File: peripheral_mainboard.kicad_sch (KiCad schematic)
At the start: 35 parts, among them J5 AudioJack3, J9 FFC Connector, SW2 SW_SPST, SW3 SW_SPST, SW7 SW_SPST, U5 TLV70033_SOT23-5, U6 PCM5102APW, U7 PAM8908

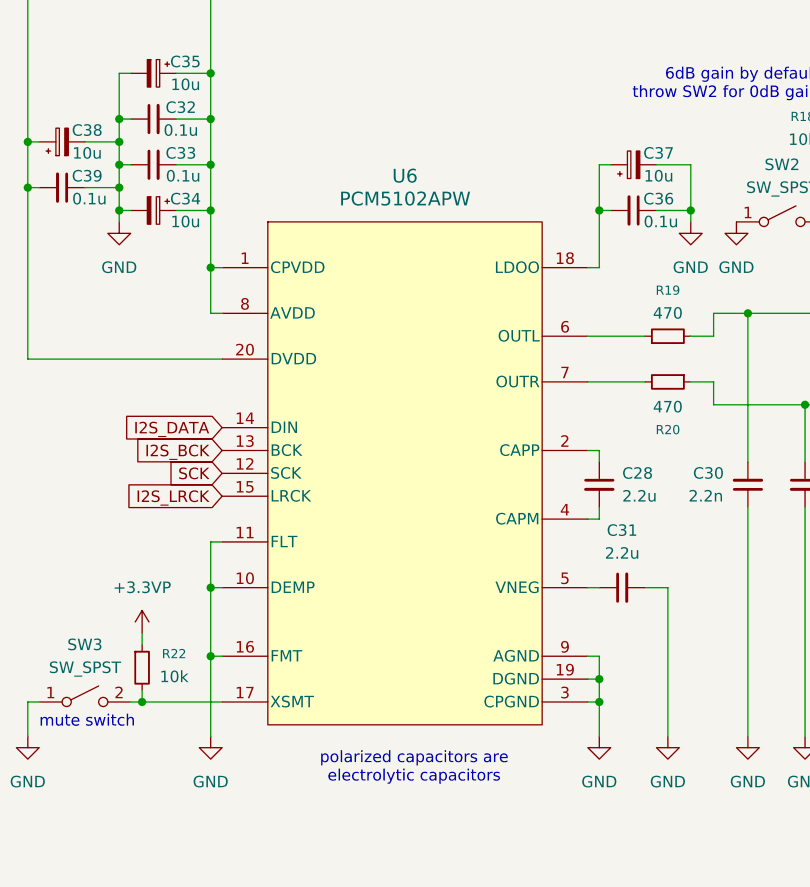
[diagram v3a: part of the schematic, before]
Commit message: removed external footprint/model
these were from ultralibrarian and should never have been included here, my bad
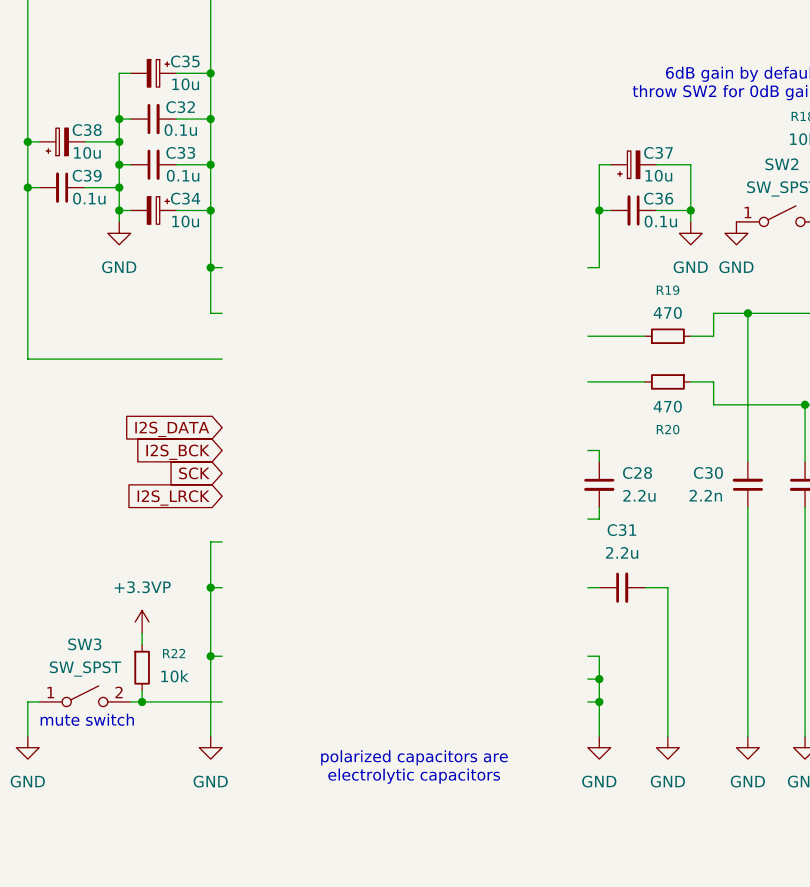
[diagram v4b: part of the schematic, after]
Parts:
- removed U6: PCM5102APW, PCM5102A:PW0020A_L, symbol PCM5102A:PCM5102APW
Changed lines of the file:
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@@
-	)
-	(symbol
-		(lib_id "PCM5102A:PCM5102APW")
-		(at 146.05 100.33 0)
-		(unit 1)
-		(exclude_from_sim no)
-		(in_bom yes)
-		(on_board yes)
-		(dnp no)
-		(fields_autoplaced yes)
-		(property "Reference" "U6"
-			(at 146.05 67.31 0)
-			(effects
-				(font
-					(size 1.524 1.524)
-				)
-			)
-		)
-		(property "Value" "PCM5102APW"
-			(at 146.05 69.85 0)
-			(effects
-				(font
-					(size 1.524 1.524)
-				)
-			)
-		)
-		(property "Footprint" "PCM5102A:PW0020A_L"
-			(at 146.05 100.33 0)
-			(effects
-				(font
-					(size 1.27 1.27)
-					(italic yes)
-				)
-				(hide yes)
-			)
-		)
-		(property "Datasheet" "PCM5102APW"
-			(at 146.05 100.33 0)
-			(effects
-				(font
-					(size 1.27 1.27)
-					(italic yes)
-				)
-				(hide yes)
-			)
-		)
-		(property "Description" ""
-			(at 146.05 100.33 0)
-			(effects
-				(font
-					(size 1.27 1.27)
-				)
-				(hide yes)
-			)
-		)
-		(pin "4"
-		)
-		(pin "14"
-		)
-		(pin "9"
-		)
-		(pin "15"
-		)
-		(pin "1"
-		)
-		(pin "5"
-		)
-		(pin "18"
-		)
-		(pin "7"
-		)
-		(pin "3"
-		)
-		(pin "8"
-		)
-		(pin "13"
-		)
-		(pin "10"
-		)
-		(pin "16"
-		)
-		(pin "19"
-		)
-		(pin "12"
-		)
-		(pin "11"
-		)
-		(pin "17"
-		)
-		(pin "20"
-		)
-		(pin "2"
-		)
-		(pin "6"
-		)
-		(instances
-			(project "Tome"
-				(path "/2c6baa8c-bfd7-43e4-8688-255743ea3ca6/4b9dfd30-3edd-45e8-9d67-c2ad4f519ba5"
-					(reference "U6")
-					(unit 1)
-				)
-			)
-		)
 	)
 	(symbol

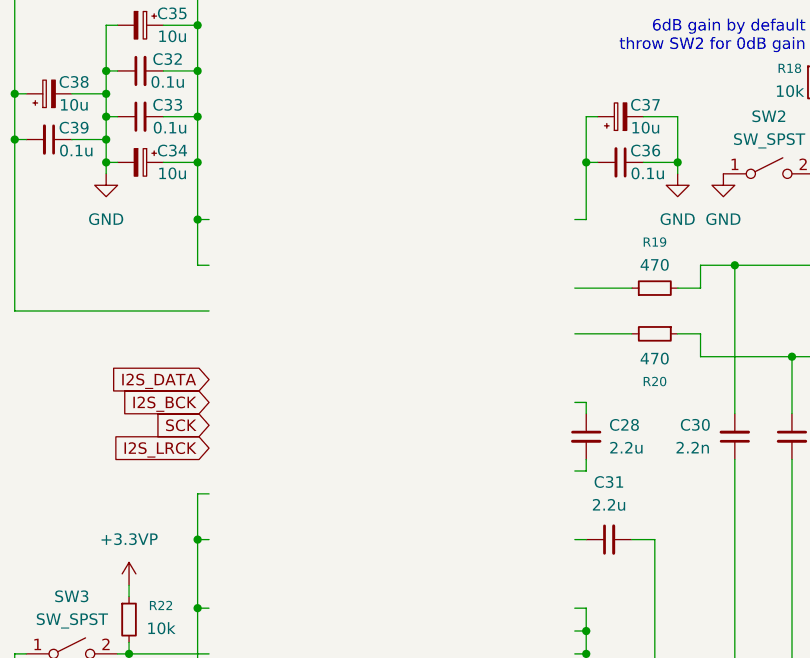
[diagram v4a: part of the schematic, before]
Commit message: replaced DAC footprint
there was literally a built-in footprint for the DAC in kicad already the whole time...
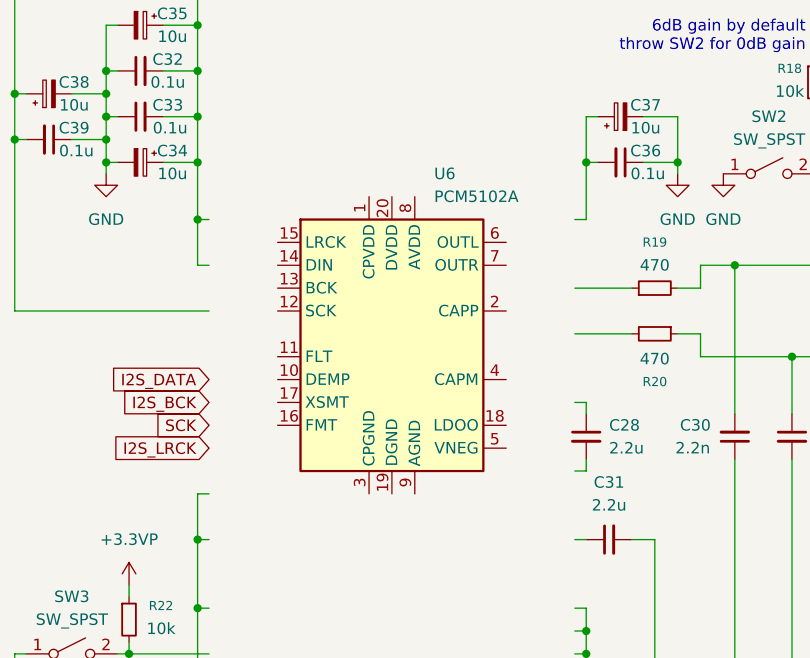
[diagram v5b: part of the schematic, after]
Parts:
- added U6: PCM5102A, Package_SO:TSSOP-20_4.4x6.5mm_P0.65mm, symbol Audio:PCM5102A
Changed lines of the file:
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@@
+	)
+	(symbol
+		(lib_id "Audio:PCM5102A")
+		(at 146.05 90.17 0)
+		(unit 1)
+		(exclude_from_sim no)
+		(in_bom yes)
+		(on_board yes)
+		(dnp no)
+		(fields_autoplaced yes)
+		(property "Reference" "U6"
+			(at 150.7333 72.39 0)
+			(effects
+				(font
+					(size 1.27 1.27)
+				)
+				(justify left)
+			)
+		)
+		(property "Value" "PCM5102A"
+			(at 150.7333 74.93 0)
+			(effects
+				(font
+					(size 1.27 1.27)
+				)
+				(justify left)
+			)
+		)
+		(property "Footprint" "Package_SO:TSSOP-20_4.4x6.5mm_P0.65mm"
+			(at 171.45 106.68 0)
+			(effects
+				(font
+					(size 1.27 1.27)
+				)
+				(hide yes)
+			)
+		)
+		(property "Datasheet" "https://www.ti.com/lit/ds/symlink/pcm5102a.pdf"
+			(at 146.05 90.17 0)
+			(effects
+				(font
+					(size 1.27 1.27)
+				)
+				(hide yes)
+			)
+		)
+		(property "Description" "2.1 VRMS, 112dB Audio Stereo DAC with PLL and 32-bit, 384kHz PCM Interface, TSSOP-20"
+			(at 146.05 90.17 0)
+			(effects
+				(font
+					(size 1.27 1.27)
+				)
+				(hide yes)
+			)
+		)
+		(pin "18"
+		)
+		(pin "14"
+		)
+		(pin "7"
+		)
+		(pin "11"
+		)
+		(pin "16"
+		)
+		(pin "9"
+		)
+		(pin "19"
+		)
+		(pin "2"
+		)
+		(pin "20"
+		)
+		(pin "4"
+		)
+		(pin "13"
+		)
+		(pin "17"
+		)
+		(pin "12"
+		)
+		(pin "15"
+		)
+		(pin "3"
+		)
+		(pin "6"
+		)
+		(pin "10"
+		)
+		(pin "1"
+		)
+		(pin "8"
+		)
+		(pin "5"
+		)
+		(instances
+			(project ""
+				(path "/2c6baa8c-bfd7-43e4-8688-255743ea3ca6/4b9dfd30-3edd-45e8-9d67-c2ad4f519ba5"
+					(reference "U6")
+					(unit 1)
+				)
+			)
+		)
 	)
 	(symbol

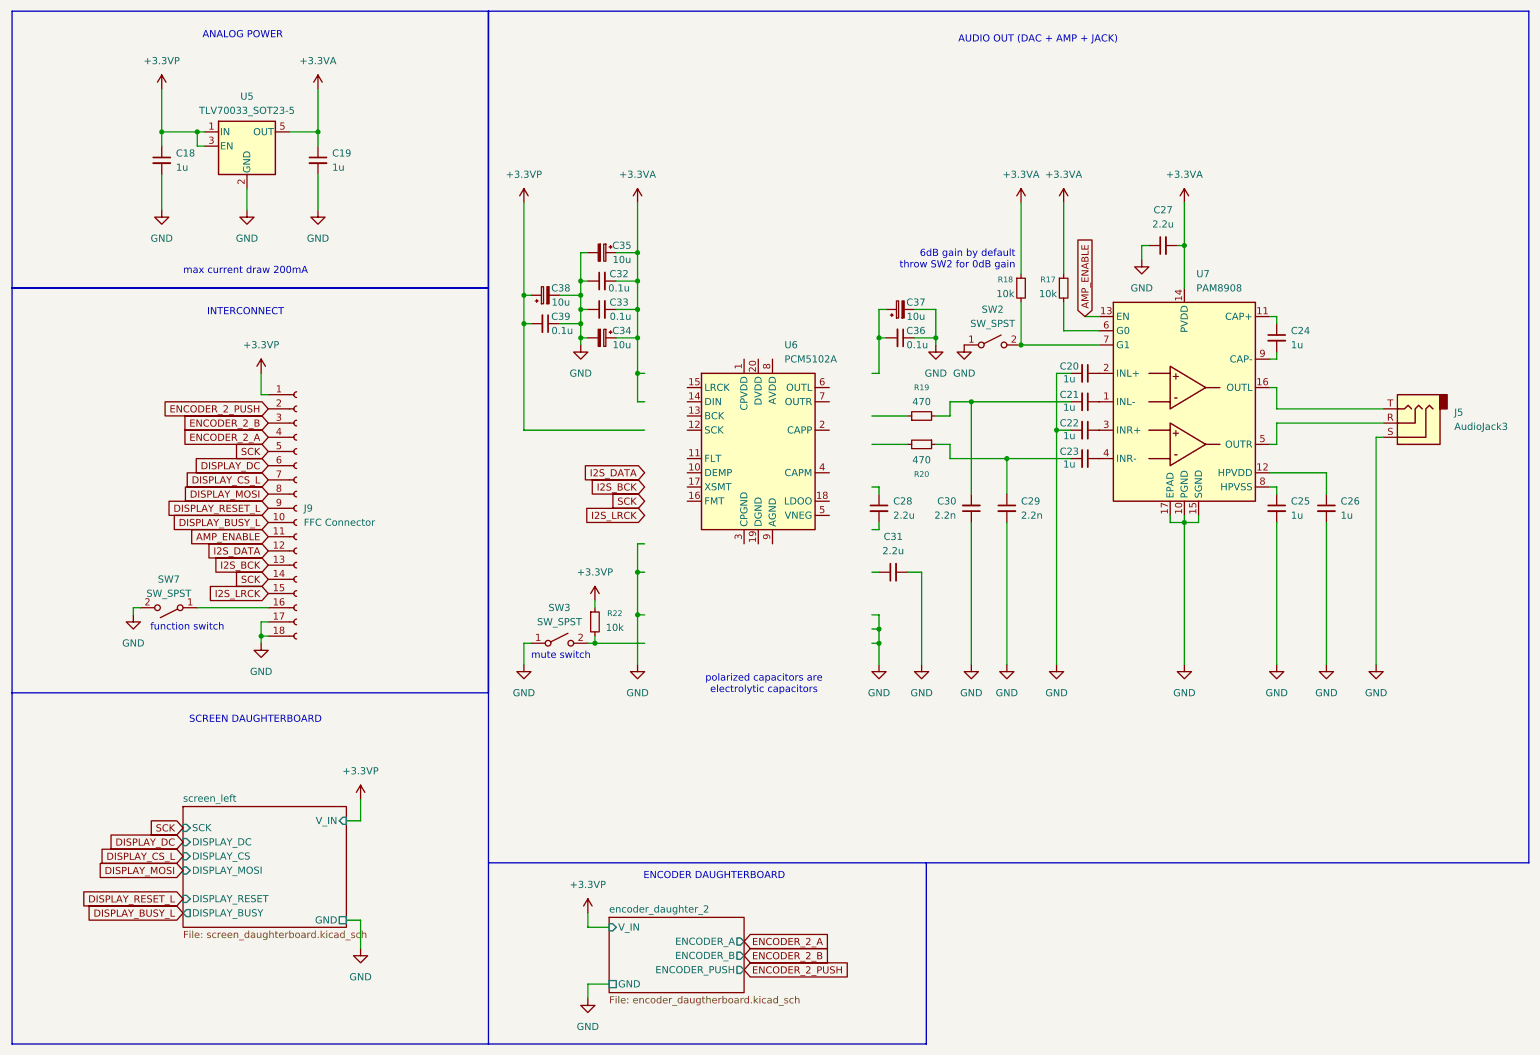
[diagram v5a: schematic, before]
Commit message: finalizing schematics
connected the new DAC footprint, filled in title blocks
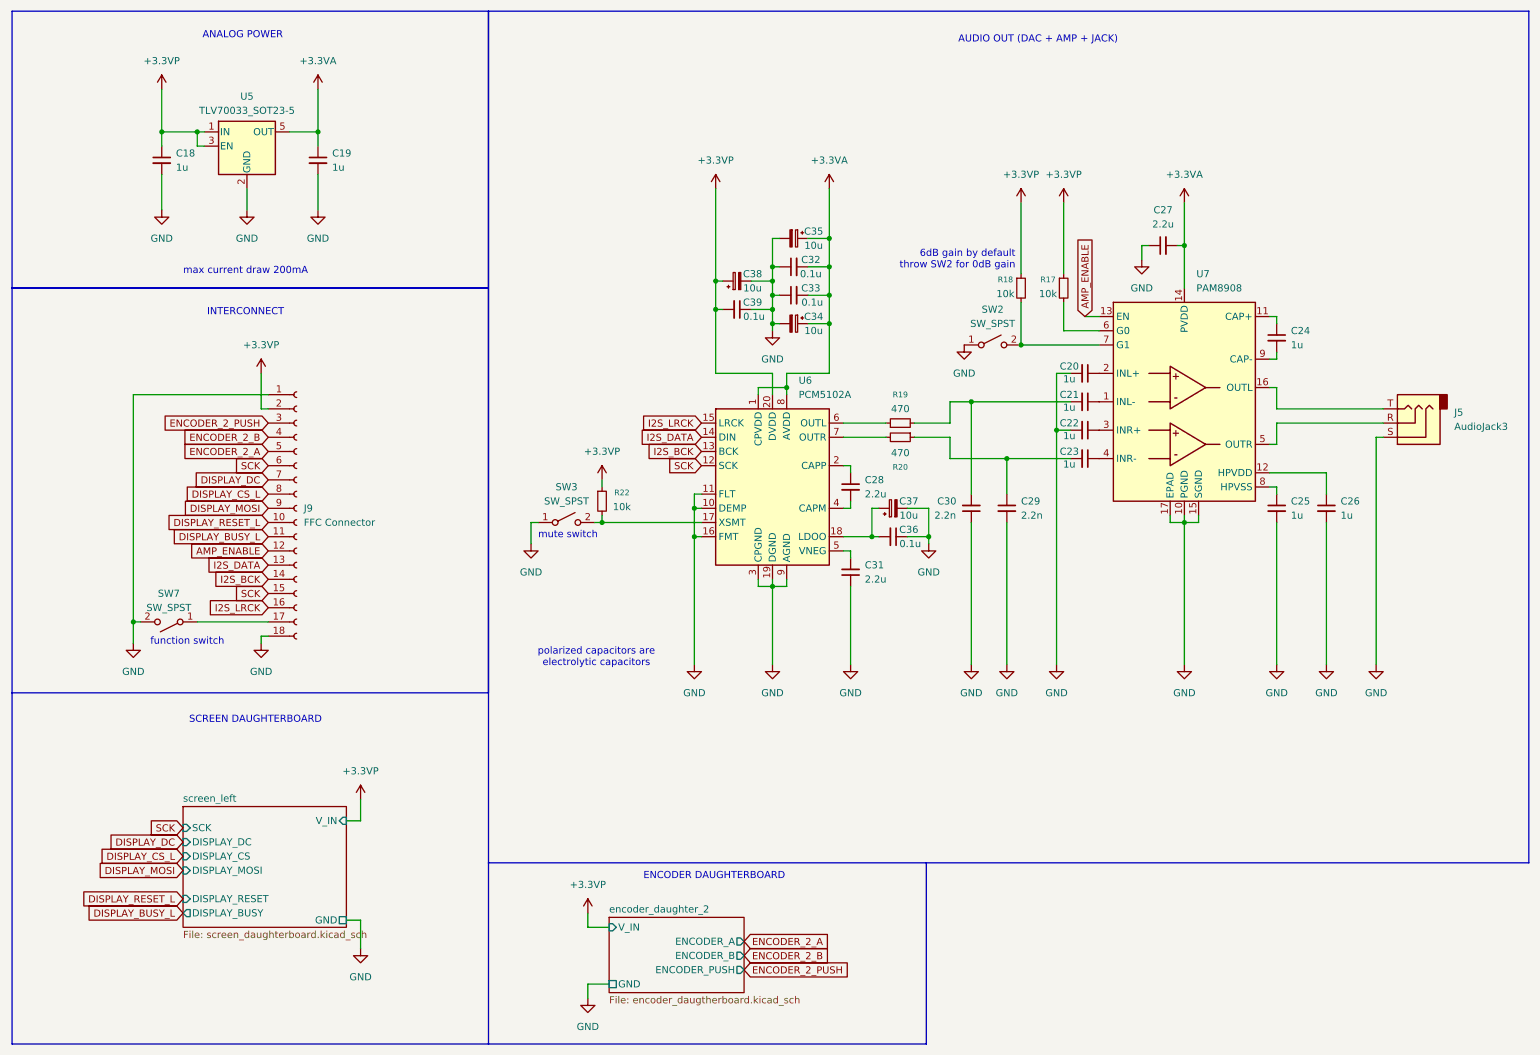
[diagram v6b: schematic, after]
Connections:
- net +3.3VA: now also U6.1 (CPVDD), U6.8 (AVDD); no longer R17.1, R18.1
- net +3.3VP: now also J9.2 (Pin_2), R17.1, R18.1, U6.20 (DVDD); no longer J9.1 (Pin_1)
- net AMP_ENABLE: now also J9.12 (Pin_12); no longer J9.11 (Pin_11)
- net DISPLAY_BUSY_L: now also J9.11 (Pin_11); no longer J9.10 (Pin_10)
- net DISPLAY_CS_L: now also J9.8 (Pin_8); no longer J9.7 (Pin_7)
- net DISPLAY_DC: now also J9.7 (Pin_7); no longer J9.6 (Pin_6)
- net DISPLAY_MOSI: now also J9.9 (Pin_9); no longer J9.8 (Pin_8)
- net DISPLAY_RESET_L: now also J9.10 (Pin_10); no longer J9.9 (Pin_9)
- net ENCODER_2_A: now also J9.5 (Pin_5); no longer J9.4 (Pin_4)
- net ENCODER_2_B: now also J9.4 (Pin_4); no longer J9.3 (Pin_3)
- net ENCODER_2_PUSH: now also J9.3 (Pin_3); no longer J9.2 (Pin_2)
- net GND: now also C31.1, J9.1 (Pin_1), U6.10 (DEMP), U6.11 (FLT), U6.16 (FMT), U6.19 (DGND), U6.3 (CPGND), U6.9 (AGND); no longer C31.2, J9.17 (Pin_17)
- net I2S_BCK: now also J9.14 (Pin_14), U6.13 (BCK); no longer J9.13 (Pin_13)
- net I2S_DATA: now also J9.13 (Pin_13), U6.14 (DIN); no longer J9.12 (Pin_12)
- net I2S_LRCK: now also J9.16 (Pin_16), U6.15 (LRCK); no longer J9.15 (Pin_15)
- net SCK: now also J9.15 (Pin_15), J9.6 (Pin_6), U6.12 (SCK); no longer J9.14 (Pin_14), J9.5 (Pin_5)
- net at R22.2, SW3.2 (B): now also U6.17 (XSMT)
- net at C28.1: now also U6.2 (CAPP)
- net at C28.2: now also U6.4 (CAPM)
- net at C36.2, C37.1: now also U6.18 (LDOO)
- net at R20.2: now also U6.7 (OUTR)
- net at SW7.1 (A): now also J9.17 (Pin_17); no longer J9.16 (Pin_16)
- net at U6.5 (VNEG): now also C31.2
- net at U6.6 (OUTL): now also R19.1
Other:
- company: (none) -> rien+la_reine;
- title: (none) -> Tome: Peripheral-Side Board
- moved on the sheet: C28, C31, C32, C33, C34, C35, C36, C37, C38, C39, R19, R20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

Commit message: assigned switch and reset button footprints
all footprints now assigned*

*will probably need something to connect the encoder daughterboard to the main boards
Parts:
- SW2, SW3, SW7: footprint (none) -> Button_Switch_SMD:SW_SPDT_CK_JS102011SAQN
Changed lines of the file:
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@@
 			)
 		)
-		(property "Footprint" ""
+		(property "Footprint" "Button_Switch_SMD:SW_SPDT_CK_JS102011SAQN"
 			(at 111.76 104.14 0)
 			(effects
@@
 			)
 		)
-		(property "Footprint" ""
+		(property "Footprint" "Button_Switch_SMD:SW_SPDT_CK_JS102011SAQN"
 			(at 187.96 72.39 0)
 			(effects
@@
 			)
 		)
-		(property "Footprint" ""
+		(property "Footprint" "Button_Switch_SMD:SW_SPDT_CK_JS102011SAQN"
 			(at 40.64 121.92 0)
 			(effects

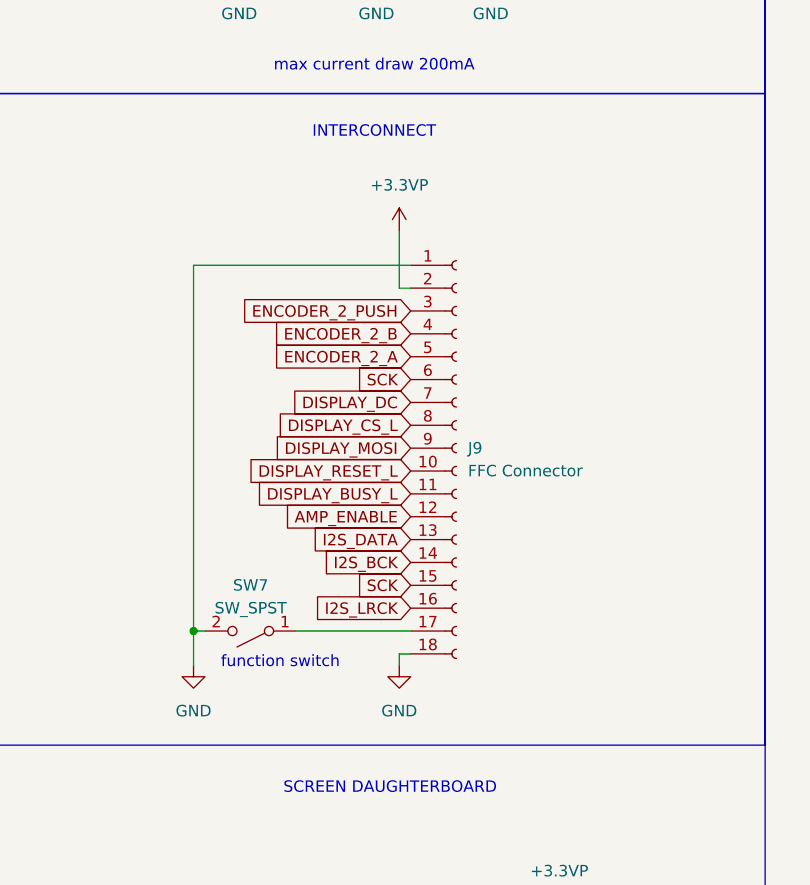
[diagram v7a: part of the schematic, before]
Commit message: update left/right interconnect
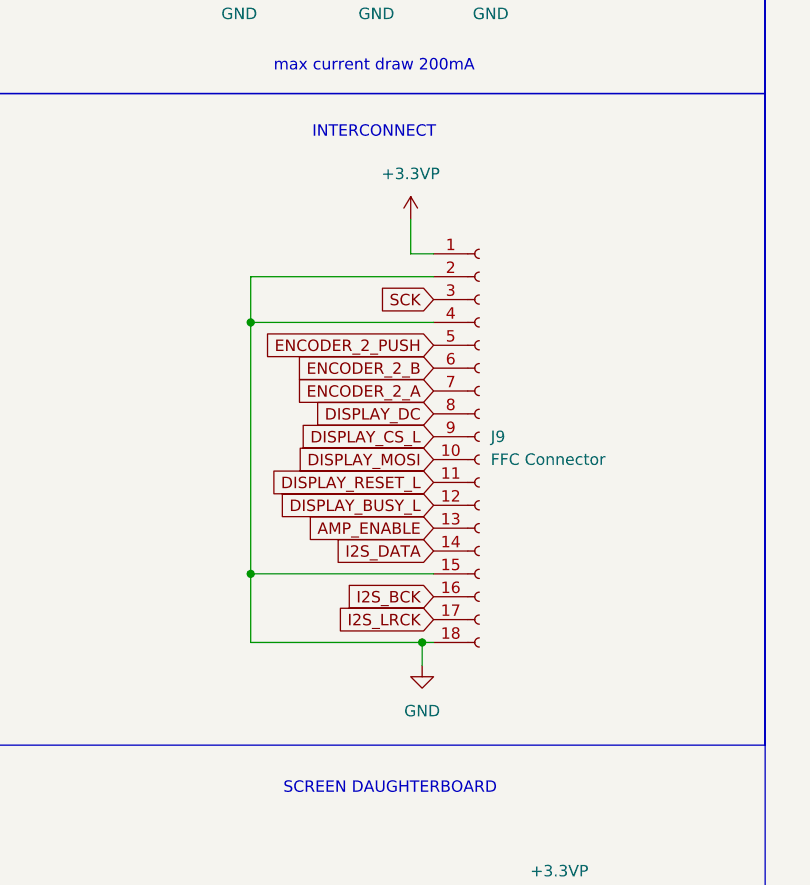
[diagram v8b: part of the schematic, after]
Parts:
- removed SW7: SW_SPST, Button_Switch_SMD:SW_SPDT_CK_JS102011SAQN, symbol Switch:SW_SPST
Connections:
- net +3.3VP: now also J9.1 (Pin_1); no longer J9.2 (Pin_2)
- net AMP_ENABLE: now also J9.13 (Pin_13); no longer J9.12 (Pin_12)
- net DISPLAY_BUSY_L: now also J9.12 (Pin_12); no longer J9.11 (Pin_11)
- net DISPLAY_CS_L: now also J9.9 (Pin_9); no longer J9.8 (Pin_8)
- net DISPLAY_DC: now also J9.8 (Pin_8); no longer J9.7 (Pin_7)
- net DISPLAY_MOSI: now also J9.10 (Pin_10); no longer J9.9 (Pin_9)
- net DISPLAY_RESET_L: now also J9.11 (Pin_11); no longer J9.10 (Pin_10)
- net ENCODER_2_A: now also J9.7 (Pin_7); no longer J9.5 (Pin_5)
- net ENCODER_2_B: now also J9.6 (Pin_6); no longer J9.4 (Pin_4)
- net ENCODER_2_PUSH: now also J9.5 (Pin_5); no longer J9.3 (Pin_3)
- net GND: now also J9.15 (Pin_15), J9.2 (Pin_2), J9.4 (Pin_4); no longer J9.1 (Pin_1)
- net I2S_BCK: now also J9.16 (Pin_16); no longer J9.14 (Pin_14)
- net I2S_DATA: now also J9.14 (Pin_14); no longer J9.13 (Pin_13)
- net I2S_LRCK: now also J9.17 (Pin_17); no longer J9.16 (Pin_16)
- net SCK: now also J9.3 (Pin_3); no longer J9.15 (Pin_15), J9.6 (Pin_6)
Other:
- note removed: "function switch"
- moved on the sheet: J9
